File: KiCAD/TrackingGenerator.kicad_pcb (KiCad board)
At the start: 2 copper layers, 102.9 x 62.2 mm, 65 parts, among them IC1 ABA-52563-BLKG, IC2 ABA-52563-BLKG, IC3 ABA-52563-BLKG, J1 Conn_Coaxial, J2 Conn_Coaxial, J3 Screw_Terminal_01x02, J4 Conn_Coaxial, M1 PAM-42, U1 L7805

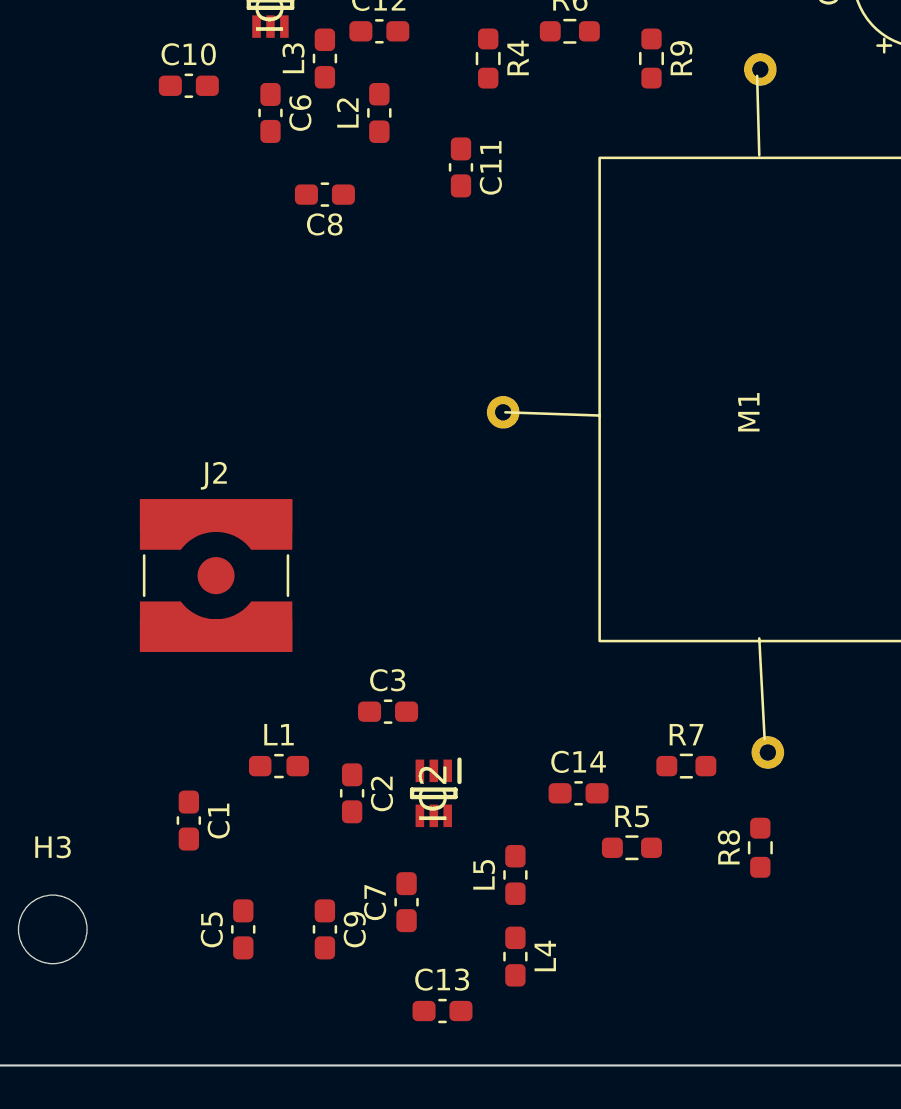
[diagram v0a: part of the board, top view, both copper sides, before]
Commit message: Changes to use LC7628 stackup
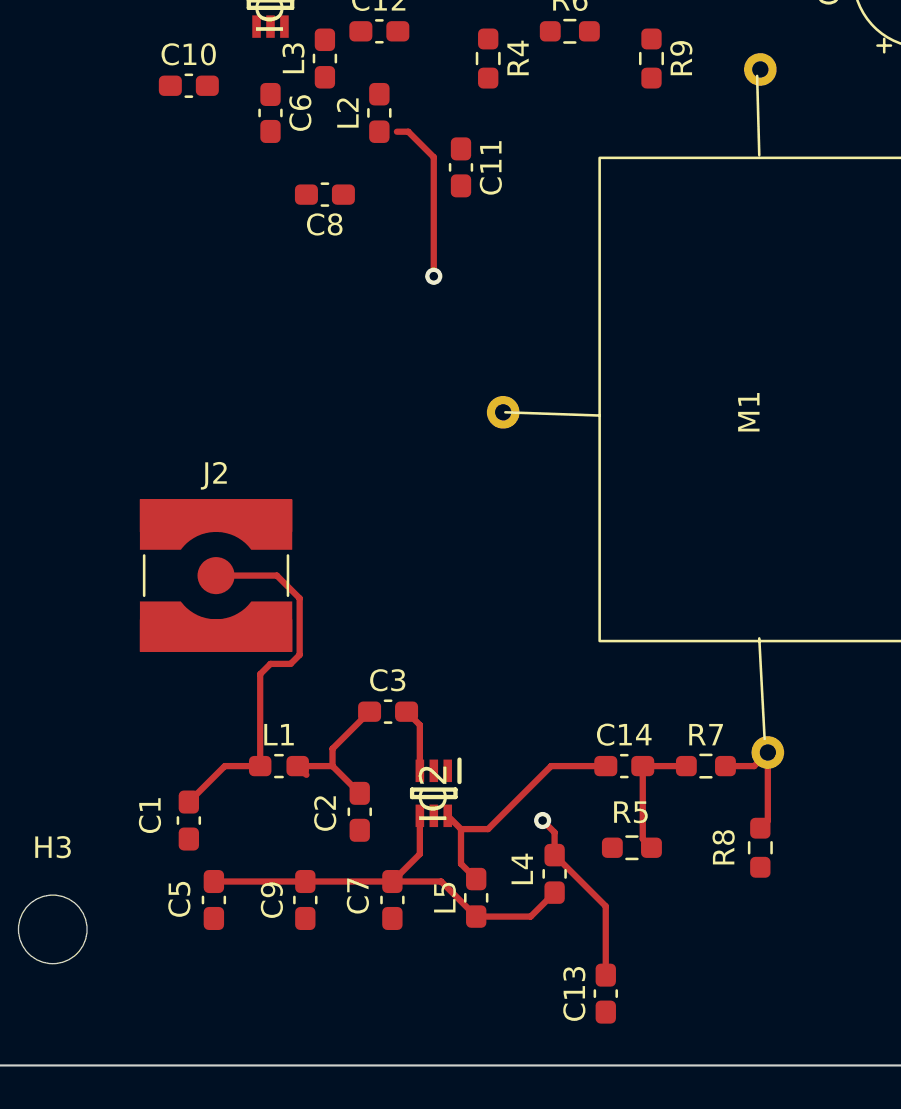
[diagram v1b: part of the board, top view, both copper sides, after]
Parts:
- moved C13 7.66 mm to (93.1, 136.3), turned to 90 degrees
- moved L4 4.27 mm to (90.7, 130.8)
- moved C14 2.48 mm to (94.0, 125.7)
- moved L5 2.12 mm to (87.1, 131.9)
- moved C5 1.94 mm to (74.8, 132.0), turned to -90 degrees
- moved C9 1.65 mm to (79.1, 132.0), turned to 90 degrees
- moved C2 0.93 mm to (81.6, 127.9)
- moved R7 0.91 mm to (97.8, 125.7)
- moved C7 0.67 mm to (83.2, 132.0), turned to -90 degrees
- turned R5 to 180 degrees
- turned R8 to -90 degrees
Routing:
- net +5V: track 0.00 -> 43.7 mm, vias 0 -> 1
- net Net-(C5-Pad1): track 0.00 -> 20.6 mm
- net Net-(C1-Pad1): track 0.00 -> 17.5 mm
- net Net-(C14-Pad1): track 0.00 -> 11.5 mm
- net Net-(C2-Pad1): track 0.00 -> 7.26 mm
- net Net-(C14-Pad2): track 0.00 -> 6.01 mm
- net Net-(R7-Pad2): track 0.00 -> 5.92 mm
- net Net-(C3-Pad2): track 0.00 -> 3.02 mm
- net (no net): vias 0 -> 1
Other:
- copper layers 2 -> 4

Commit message: More routing work
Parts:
- J1, J2, J4: footprint Connector_Coaxial:SMA_Amphenol_132134-10_Vertical -> Connector_Coaxial:SMA_Amphenol_132289_EdgeMount
- moved H3 23.7 mm to (85.1, 117.7)
- moved J3 21.3 mm to (139.6, 88.3), turned to 0 degrees
- moved R13 10.8 mm to (141.7, 97.1)
- moved H2 10.6 mm to (149.7, 88.0)
- moved H4 10.1 mm to (148.7, 133.1)
- moved H1 8.83 mm to (75.9, 80.5)
- moved J1 8.16 mm to (90.3, 80.6), turned to 90 degrees
- moved J4 6.02 mm to (151.4, 120.4)
- moved IC3 5.59 mm to (130.6, 112.2)
- moved C26 5.41 mm to (141.5, 114.9), turned to 90 degrees
- moved L7 5.30 mm to (133.1, 117.3)
- moved C24 5.06 mm to (128.3, 122.5)
- moved C25 5.03 mm to (138.5, 111.7)
- moved C20 4.88 mm to (138.6, 122.1)
- moved L8 4.57 mm to (138.9, 116.8)
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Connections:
- H1 pad : GNDPWR -> (no net)
- H2 pad : GNDPWR -> (no net)
- H3 pad : GNDPWR -> (no net)
- H4 pad : GNDPWR -> (no net)
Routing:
- net +5V: track 43.7 -> 15.8 mm, vias 1 -> 3
- net Net-(J4-Pad1): track 0.00 -> 16.9 mm
- net Net-(J1-Pad1): track 0.00 -> 9.68 mm
- net Net-(M1-Pad1): track 0.00 -> 8.71 mm
- net Net-(M1-Pad4): track 0.00 -> 6.43 mm
- net Net-(C15-Pad2): track 0.00 -> 3.05 mm
- net Net-(C1-Pad1): track 17.5 -> 19.2 mm
- net GNDPWR: track 0.00 -> 1.62 mm
- net (no net): vias 1 -> 0
- added copper zone on In1.Cu, net +5V
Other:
- board size 102.9 x 62.2 mm -> 84.4 x 60.3 mm

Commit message: Add more routing
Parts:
- moved H1 1.75 mm to (74.4, 81.3)
- moved J2 1.39 mm to (73.5, 116.9)
- moved L8 0.99 mm to (138.0, 117.0), turned to 90 degrees
- turned C12 to 180 degrees
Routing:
- net Net-(C22-Pad1): track 0.00 -> 25.2 mm
- net Net-(C19-Pad1): track 0.00 -> 18.9 mm
- net Net-(C10-Pad2): track 0.00 -> 18.1 mm
- net Net-(C25-Pad1): track 0.00 -> 15.4 mm
- net Net-(C16-Pad1): track 0.00 -> 13.6 mm
- net Net-(C25-Pad2): track 0.00 -> 10.7 mm
- net Net-(C17-Pad2): track 0.00 -> 9.29 mm
- net Net-(C4-Pad1): track 0.00 -> 9.22 mm
- net Net-(C15-Pad2): track 3.05 -> 12.1 mm
- net +12V: track 0.00 -> 8.98 mm
- net GNDPWR: track 1.62 -> 9.52 mm
- net Net-(C12-Pad1): track 0.00 -> 7.41 mm
- net +5V: track 15.8 -> 22.0 mm
- net Net-(C12-Pad2): track 0.00 -> 3.99 mm
- net Net-(C4-Pad2): track 0.00 -> 2.85 mm
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- added copper zone on In2.Cu, net +5V
- added copper zone on B.Cu, net GNDPWR
- added copper zone on F.Cu, net GNDPWR
- added copper zone on In1.Cu, net GNDPWR
- removed copper zone on In1.Cu, net +5V

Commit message: Further updates
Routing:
- net GNDPWR: track 9.52 -> 15.8 mm
- net Net-(C2-Pad1): track 7.26 -> 6.68 mm
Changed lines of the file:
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@@
   )
   (gr_rect (start 70.2564 77.47) (end 154.6352 137.7696) (layer "Edge.Cuts") (width 0.1) (fill none))
+  (segment (start 77.47 89.12) (end 77.47 91.22) (width 0.29337) (layer "F.Cu") (net 1))
+  (segment (start 130.556 113.027796) (end 130.659804 113.1316) (width 0.29337) (layer "F.Cu") (net 1))
   (segment (start 113.03 92.3025) (end 119.38 85.9525) (width 0.25) (layer "F.Cu") (net 1))
   (segment (start 119.38 85.9525) (end 119.38 85.415) (width 0.25) (layer "F.Cu") (net 1))
+  (segment (start 130.556 111.1164) (end 130.556 113.027796) (width 0.29337) (layer "F.Cu") (net 1))
+  (segment (start 85.09 125.95) (end 85.09 128.05) (width 0.29337) (layer "F.Cu") (net 1))
   (segment (start 73.66 127.4075) (end 75.3375 125.73) (width 0.29337) (layer "F.Cu") (net 2))
   (segment (start 76.72 116.84) (end 78.902498 119.022498) (width 0.29337) (layer "F.Cu") (net 2))
@@
   (segment (start 78.902498 119.022498) (end 78.902498 123.817502) (width 0.29337) (layer "F.Cu") (net 2))
   (segment (start 75.3375 125.73) (end 76.99 125.73) (width 0.29337) (layer "F.Cu") (net 2))
-  (segment (start 79.1475 126.1375) (end 78.74 125.73) (width 0.29337) (layer "F.Cu") (net 3))
   (segment (start 80.3645 125.73) (end 80.3645 124.9205) (width 0.29337) (layer "F.Cu") (net 3))
   (segment (start 80.3645 124.9205) (end 82.095 123.19) (width 0.29337) (layer "F.Cu") (net 3))
@@
   (segment (start 91.1227 129.8842) (end 90.7288 129.8842) (width 0.29337) (layer "F.Cu") (net 9))
   (segment (start 84.8246 96.125) (end 84.836 96.1136) (width 0.29337) (layer "F.Cu") (net 9))
-  (via micro (at 130.4036 120.3452) (size 0.8) (drill 0.4) (layers "F.Cu" "In2.Cu") (remove_unused_layers) (free) (net 9))
-  (via micro (at 84.836 96.1136) (size 0.8) (drill 0.4) (layers "F.Cu" "In2.Cu") (remove_unused_layers) (free) (net 9))
+  (via micro (at 130.4036 120.3452) (size 0.8) (drill 0.4) (layers "F.Cu" "In2.Cu") (remove_unused_layers) (keep_end_layers) (free) (net 9))
+  (via blind (at 84.836 96.1136) (size 0.8) (drill 0.4) (layers "F.Cu" "In2.Cu") (remove_unused_layers) (free) (net 9))
   (via micro (at 90.17 128.27) (size 0.8) (drill 0.4) (layers "F.Cu" "In2.Cu") (remove_unused_layers) (free) (net 9))
   (segment (start 80.01 91.835) (end 81.2925 91.835) (width 0.25) (layer "F.Cu") (net 10))
@@
   (segment (start 115.57 109.5775) (end 118.11 109.5775) (width 0.29337) (layer "F.Cu") (net 26))
   (zone (net 1) (net_name "GNDPWR") (layer "F.Cu") (hatch edge 0.508)
-    (connect_pads (clearance 0.508))
+    (connect_pads yes (clearance 0.508))
     (min_thickness 0.254) (filled_areas_thickness no)
     (fill yes (thermal_gap 0.508) (thermal_bridge_width 0.508))
@@
   )
   (zone (net 1) (net_name "GNDPWR") (layer "In1.Cu") (hatch edge 0.508)
-    (connect_pads (clearance 0.508))
+    (connect_pads yes (clearance 0.508))
     (min_thickness 0.254) (filled_areas_thickness no)
     (fill yes (thermal_gap 0.508) (thermal_bridge_width 0.508))
@@
   )
   (zone (net 1) (net_name "GNDPWR") (layer "B.Cu") (hatch edge 0.508)
-    (connect_pads (clearance 0.508))
+    (connect_pads yes (clearance 0.508))
     (min_thickness 0.254) (filled_areas_thickness no)
     (fill yes (thermal_gap 0.508) (thermal_bridge_width 0.508))

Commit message: New Branch for Richard's Ideas
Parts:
- moved C16 11.3 mm to (127.8, 110.1)
- moved J4 9.11 mm to (151.9, 111.3)
- moved C17 8.81 mm to (130.7, 109.2), turned to 0 degrees
- moved C15 7.73 mm to (122.2, 110.1)
- moved L6 7.30 mm to (125.0, 109.2)
- moved C26 6.84 mm to (137.3, 109.5), turned to 0 degrees
- moved R16 5.37 mm to (145.6, 112.2)
- moved C24 5.08 mm to (131.9, 118.9), turned to 0 degrees
- moved C19 4.94 mm to (138.3, 118.0)
- moved C20 4.62 mm to (136.5, 118.0)
- moved R15 4.53 mm to (142.8, 111.2)
- moved C18 4.45 mm to (130.7, 107.4), turned to 0 degrees
- moved IC3 4.10 mm to (134.2, 110.2)
- moved C21 4.09 mm to (132.4, 114.0)
- moved R14 3.44 mm to (140.2, 112.2)
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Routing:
- net Net-(C22-Pad1): track 25.2 -> 0.00 mm
- net Net-(C5-Pad1): track 20.6 -> 0.00 mm
- net Net-(C10-Pad2): track 18.1 -> 0.00 mm
- net +5V: track 22.0 -> 5.06 mm, vias 3 -> 2
- net Net-(C1-Pad1): track 16.4 -> 0.00 mm
- net Net-(C14-Pad1): track 11.5 -> 0.00 mm
- net GNDPWR: track 15.8 -> 5.93 mm, vias 0 -> 127
- net Net-(J1-Pad1): track 9.68 -> 0.00 mm
- net Net-(C4-Pad1): track 9.22 -> 0.00 mm
- net +12V: track 8.98 -> 0.00 mm
- net Net-(M1-Pad1): track 8.71 -> 0.00 mm
- net Net-(J4-Pad1): track 16.9 -> 8.38 mm
- net Net-(C16-Pad1): track 13.6 -> 5.76 mm
- net Net-(C25-Pad1): track 15.4 -> 7.71 mm
- net Net-(C12-Pad1): track 7.41 -> 0.00 mm
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
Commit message: Further work compacting and tidying
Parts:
- moved J1 20.9 mm to (73.2, 92.7), turned to 180 degrees
- moved C13 19.1 mm to (88.0, 115.5)
- moved C9 18.0 mm to (86.3, 115.5), turned to -90 degrees
- moved C10 17.4 mm to (86.2, 81.9), turned to -90 degrees
- moved C5 16.9 mm to (86.3, 119.5)
- moved C11 16.4 mm to (93.9, 83.2), turned to 0 degrees
- moved H3 15.7 mm to (80.9, 132.8)
- moved R1 14.5 mm to (77.1, 93.6)
- moved C8 13.8 mm to (83.5, 85.8), turned to -90 degrees
- moved C7 13.5 mm to (88.2, 119.5)
- moved L4 13.0 mm to (89.9, 117.8)
- moved L2 13.0 mm to (89.2, 84.0), turned to -90 degrees
- moved C6 12.9 mm to (86.2, 85.8)
- moved L5 11.0 mm to (90.0, 121.3), turned to -90 degrees
- moved IC1 10.8 mm to (88.1, 92.1), turned to 0 degrees
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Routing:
- net +5V: track 5.06 -> 36.8 mm, vias 2 -> 3
- net Net-(C22-Pad1): track 0.00 -> 29.3 mm
- net Net-(C10-Pad2): track 0.00 -> 16.8 mm
- net Net-(C5-Pad1): track 0.00 -> 14.2 mm
- net +12V: track 0.00 -> 13.1 mm
- net Net-(C1-Pad1): track 0.00 -> 5.59 mm
- net Net-(J1-Pad1): track 0.00 -> 5.54 mm
- net Net-(C12-Pad2): track 0.00 -> 4.10 mm
- net Net-(C14-Pad1): track 0.00 -> 3.85 mm
- net Net-(M1-Pad1): track 0.00 -> 3.76 mm
- net Net-(C12-Pad1): track 0.00 -> 3.53 mm
- net Net-(M1-Pad3): track 0.00 -> 3.52 mm
- net Net-(C2-Pad1): track 0.00 -> 3.28 mm
- net Net-(C14-Pad2): track 0.00 -> 3.26 mm
- net Net-(C4-Pad1): track 0.00 -> 2.44 mm
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
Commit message: Further routing and stitching
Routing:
- net GNDPWR: track 5.93 -> 17.1 mm, vias 129 -> 258
